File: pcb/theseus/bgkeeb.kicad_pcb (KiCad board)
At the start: 2 copper layers, 99.1 x 90.5 mm, 108 parts, among them J1 Pimoroni, SW1 SW_Push, SW11 SW_Push, SW12 SW_Push, SW13 SW_Push, SW14 SW_Push, SW15 SW_Push, SW2 SW_Push, SW21 SW_Push, SW22 SW_Push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

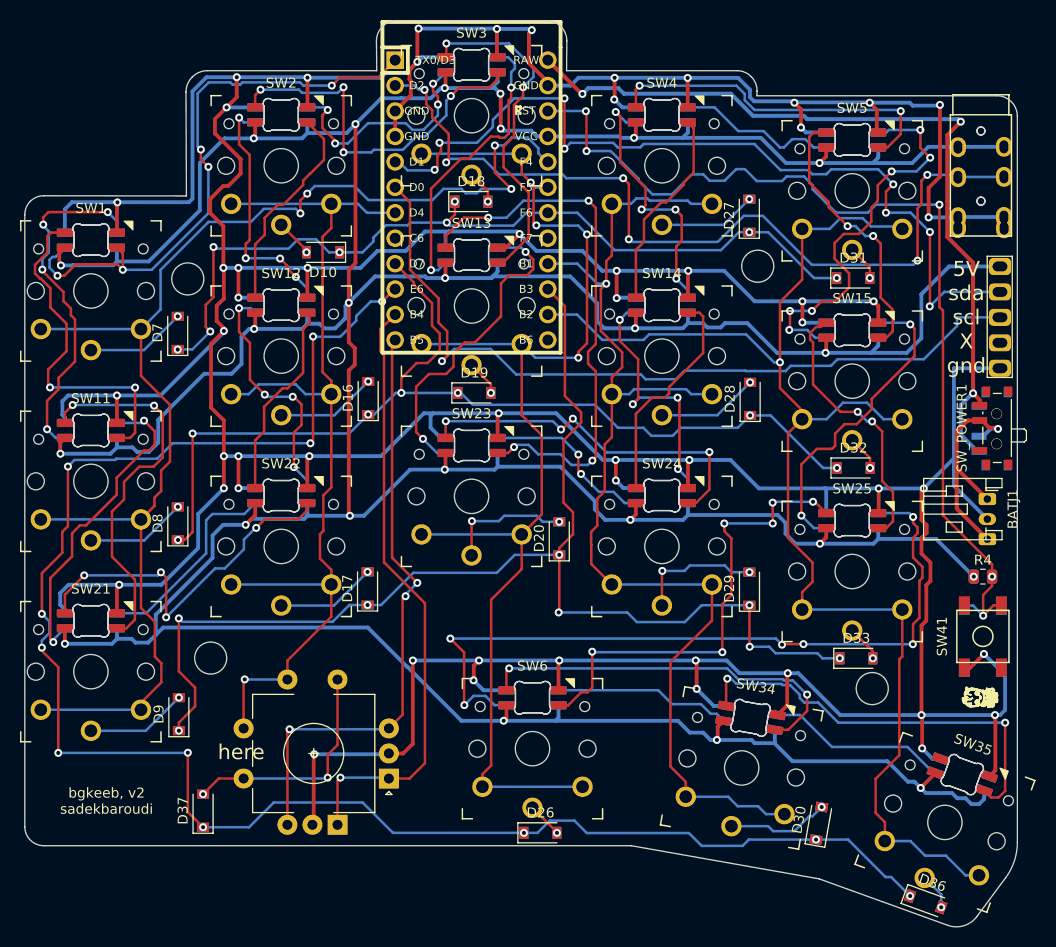
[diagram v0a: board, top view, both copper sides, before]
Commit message: Bye Promicro, Hello RP2040-Zero (with Xiao compatibility... almost!)
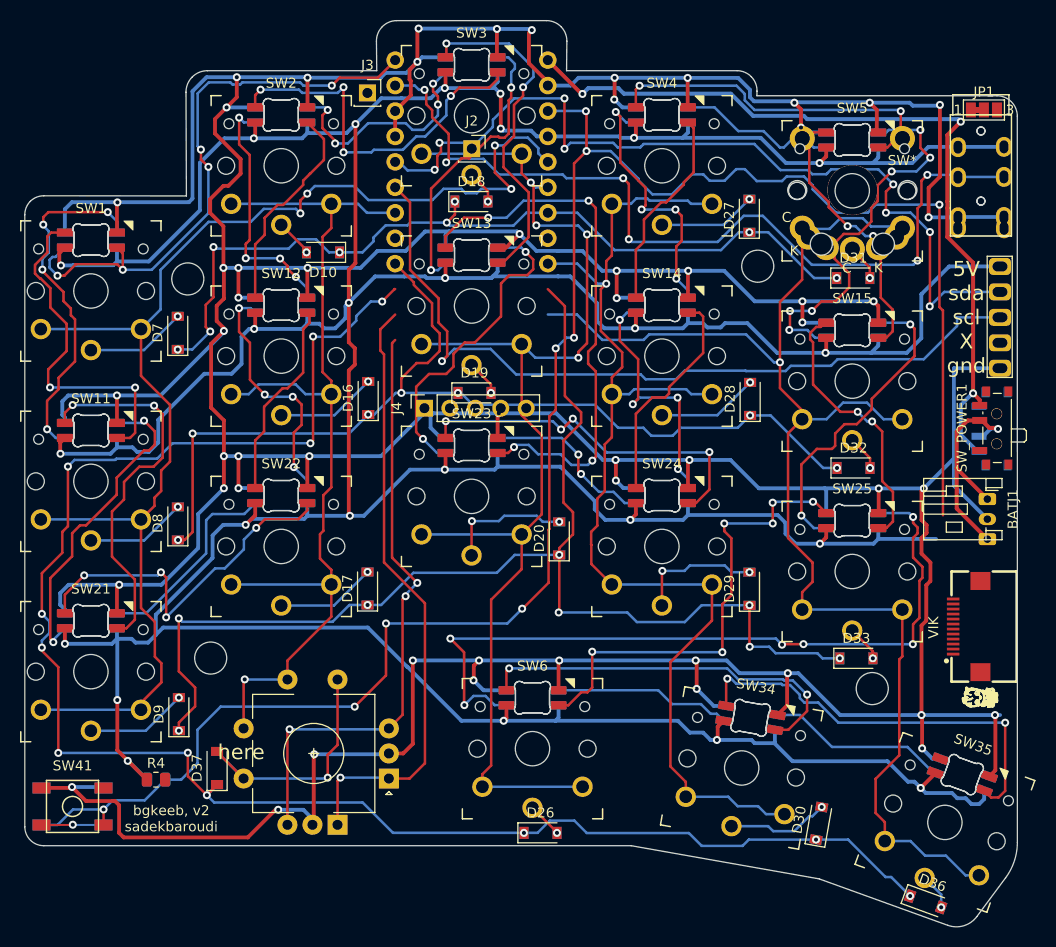
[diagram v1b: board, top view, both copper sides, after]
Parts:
- added J2: Bat+ pth, Connector_PinSocket_2.54mm:PinSocket_1x01_P2.54mm_Vertical, F.Cu at (99.0, 43.8)
- added J3: reset pth, Connector_PinSocket_2.54mm:PinSocket_1x01_P2.54mm_Vertical, F.Cu at (88.6, 38.3)
- added J4: rp2040-zero-tht-bottom-bodged, Connector_PinSocket_2.54mm:PinSocket_1x05_P2.54mm_Vertical, F.Cu at (94.3, 69.7)
- added J5: ~, fingerpunch:vik-connector-horizontal, F.Cu at (149.1, 91.5)
- added JP1: SolderJumper_3_Bridged12, Jumper:SolderJumper-3_P1.3mm_Bridged12_Pad1.0x1.5mm_NumberLabels, F.Cu at (150.1, 40.0)
- added SW*: SW_PUSH, theseus:pg1353-ks27, F.Cu at (137.0, 48.0)
- U1: value ProMicro -> rp2040-zero-tht-sides; footprint Keebio-Parts:ArduinoProMicro -> theseus:rp2040-zero-tht-nocut; moved to B.Cu
- moved SW41 92.5 mm to (59.2, 109.5), turned to 180 degrees
- moved SW8 92.4 mm to (59.2, 109.5), turned to 0 degrees
- moved R4 85.0 mm to (67.5, 106.8)
- moved R1 85.0 mm to (67.5, 106.8)
- moved D37 4.49 mm to (73.6, 105.6)
- moved D81 4.49 mm to (73.6, 105.6)
- moved U1 3.81 mm to (99.0, 45.1), turned to 180 degrees
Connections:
- SW_POWER1 pad 3: raw -> Bat+ Pad
- U1 pad 15: row2 -> sda
- U1 pad 16: col3 -> scl
- U1 pad 17: unconnected-(U1-A0/PF7-Pad17) -> col3
- U1 pad 18: row0 -> col2
- U1 pad 19: col2 -> col1
- U1 pad 2: data -> col4
- U1 pad 21: +5V -> +3.3V
- U1 pad 22: RESET -> GND
- U1 pad 23: GND -> +5V
- U1 pad 3: GND -> row0
- U1 pad 4: GND -> row1
- U1 pad 5: sda -> row2
- U1 pad 6: scl -> row3
- U1 pad 7: col1 -> data
- U1 pad 8: unconnected-(U1-5/PC6-Pad8) -> ENC1A
- U1 pad 9: row1 -> ENC1B
- U3 pad 4: +5V -> Net-(JP1-C)
- U4 pad 4: +5V -> Net-(JP1-C)
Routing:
- net RESET: track 97.4 -> 193.0 mm, vias 5 -> 9
- net (no net): track 0.00 -> 88.2 mm, vias 0 -> 4
- net raw: track 81.9 -> 0.00 mm, vias 3 -> 0
- net GND: track 646.9 -> 673.3 mm, vias 53 -> 54
- net +5V: track 521.5 -> 534.2 mm, vias 24 -> 25
- net Net-(D37-A): track 23.3 -> 26.2 mm, vias 2 -> 1
- net row3: track 175.4 -> 174.2 mm
